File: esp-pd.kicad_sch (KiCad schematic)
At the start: 84 parts, among them J1 USB C Power, J2 USB C Data, J3 Power Out, J4 ESP PD Board pins, Q1 IRF7416, Q2 MMBT3904, SW1 Boot, SW2 Reset, SW3 Up, SW4 Down, SW5 VBUS Switch, U1 ESP32-C3, U2 FUSB302MPX, U3 TPD4E05U06DQA, U4 ME6217C33M5G, U5 MP9943GQ-Z, Y1 40 MHz

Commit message: refactored
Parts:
- removed C13, C14, C15: 10 uF, symbol Device:C
- removed C16, C28: 0.1 uF, symbol Device:C
- removed C19: 22 uF, symbol Device:C
- removed C3, C4: C, symbol Device:C
- removed C5: 1 uF, symbol Device:C
- removed R1, R2: 5.1K, symbol Device:R
- removed R17: 4.7K, symbol Device:R
- removed R18: 1K, symbol Device:R
- removed R19: 1k, symbol Device:R
- removed R20: 10k, symbol Device:R
- removed R7, R8: 10K, symbol Device:R
- added C13, C14, C15: 10 uF, symbol Device:C_Small
- added C16, C4: 0.1 uF, symbol Device:C_Small
- added C3: ~, symbol Device:C_Small
- added C33: 22 uF, symbol Device:C_Small
- added C5: 1 uF, symbol Device:C_Small
- added R1, R8: 5.1k, symbol Device:R_Small
- added R18, R27: 1k, symbol Device:R_Small
- added R19: 10k, symbol Device:R_Small
- added R20: 4.7k, symbol Device:R_Small
- C31: value 1 uF -> ~; now not fitted
- R26: now not fitted
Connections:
- net +5V: now also C13.2, C33.2; no longer C31.2
- net ADC_VBUS: now also C4.2
- net ESP_EN: now also C5.1
- net GND: now also C31.2, J1.S1 (SHIELD), J2.S1 (SHIELD), C13.1, C14.1, C15.1, C16.1, C3.2, C33.1, C4.1, C5.2, R1.2, R19.1, R8.1; no longer C31.1
- net INT: now also R4.1; no longer R6.1
- net MOS_EN: now also R18.1
- net SDA: now also R6.1; no longer R4.1
- net VBUS: now also C15.2, C16.2, R20.1; no longer R10.1
- net VCC: now also R23.1, C14.2; no longer R23.2
- net at L1.1: now also AE1.1 (FEED), C31.1; no longer U1.1 (LNA_IN)
- net at SW5.1, U2.2 (VBUS): now also R10.1
- net D-: now reaches J2.A7 (D-), J2.B7 (D-)
- net D-: now also R25.2, U3.4 (D2+); no longer R24.1, U3.2 (D1-)
- net at Q2.1 (B): now also R18.2, R19.2
- net D+: now reaches J2.A6 (D+), J2.B6 (D+)
- net D+: now also R24.1, U3.5 (D2-); no longer R25.2, U3.1 (D1+)
- net CC1: now reaches J1.A5 (CC1), U2.10 (CC1), U2.11 (CC1)
- net CC1: now also U3.1 (D1+); no longer U3.4 (D2+)
- net CC2: now reaches J1.B5 (CC2), U2.1 (CC2), U2.14 (CC2)
- net CC2: now also U3.2 (D1-); no longer U3.5 (D2-)
- net ANT: now reaches L1.2
- net ANT: now also U1.1 (LNA_IN), C3.1; no longer AE1.1 (FEED)
- net at D2.1 (A), Q1.4 (G): now also R20.2, R27.1
- net at U5.1 (FB): now also R15.2; no longer R15.1
- net at R26.1, U5.8 (PG): now also R23.2; no longer R23.1
- net at J2.B5 (CC2): now also R8.2
- net VOUT: now reaches J3.2 (_VMOS), Q1.5 (D), Q1.6 (D), Q1.7 (D), Q1.8 (D)
- net at J2.A5 (CC1): now also R1.1
- net at C20.1, R14.1, R16.2: now also R15.1; no longer R15.2
- net at Q2.3 (C): now also R27.2
- net Power Good renamed GPIO0
- net SSD_RST: no longer names the net of C27.1, D4.2 (A), OLED1.14 (~{RES}), R22.2
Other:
- note added: "3.3V LDO"
- note added: "5V Buck Regulator"
- note added: "Antenna"
- note added: "Buttons and LED"
- note added: "Connectors"
- note added: "Display"
- note added: "ESP32-C3"
- note added: "For I2C, FUSB INT and ESP32-C3 strapping pins"
- note added: "Pull-ups"
- note added: "USB Data + TVS"
- note added: "USB Power Delivery"
- note added: "VOUT Mosfet"
- moved on the sheet: AE1, C1, C10, C11, C12, C17, C18, C2, C20, C21, C22, C23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

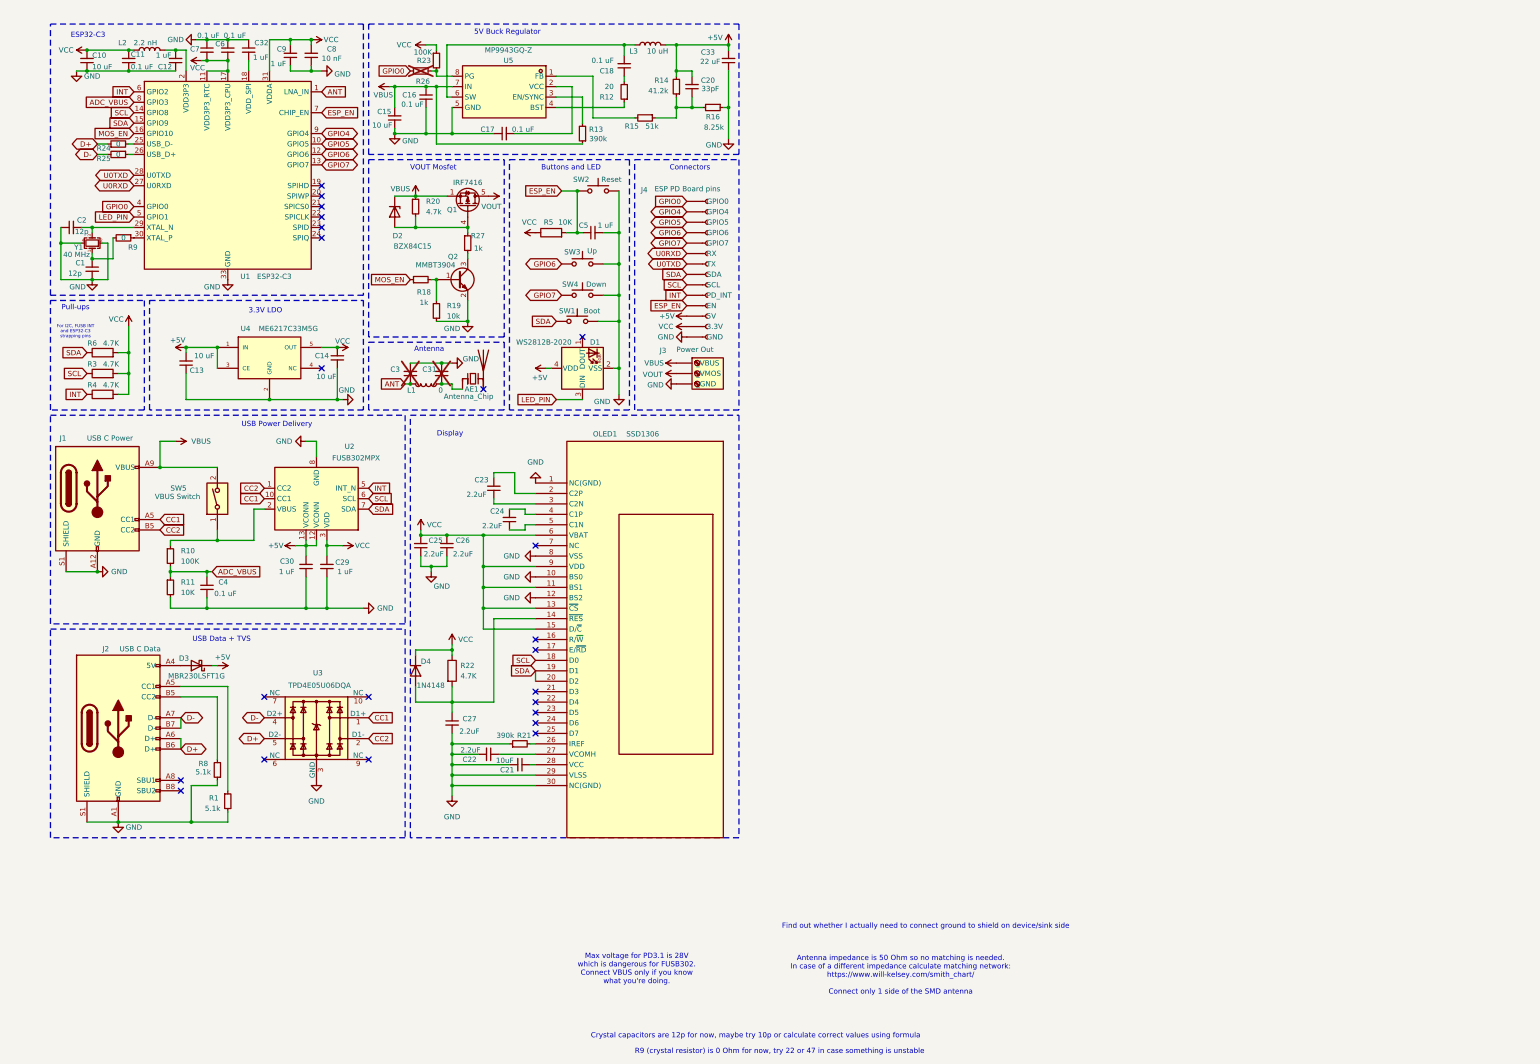
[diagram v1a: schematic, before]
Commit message: A4 format
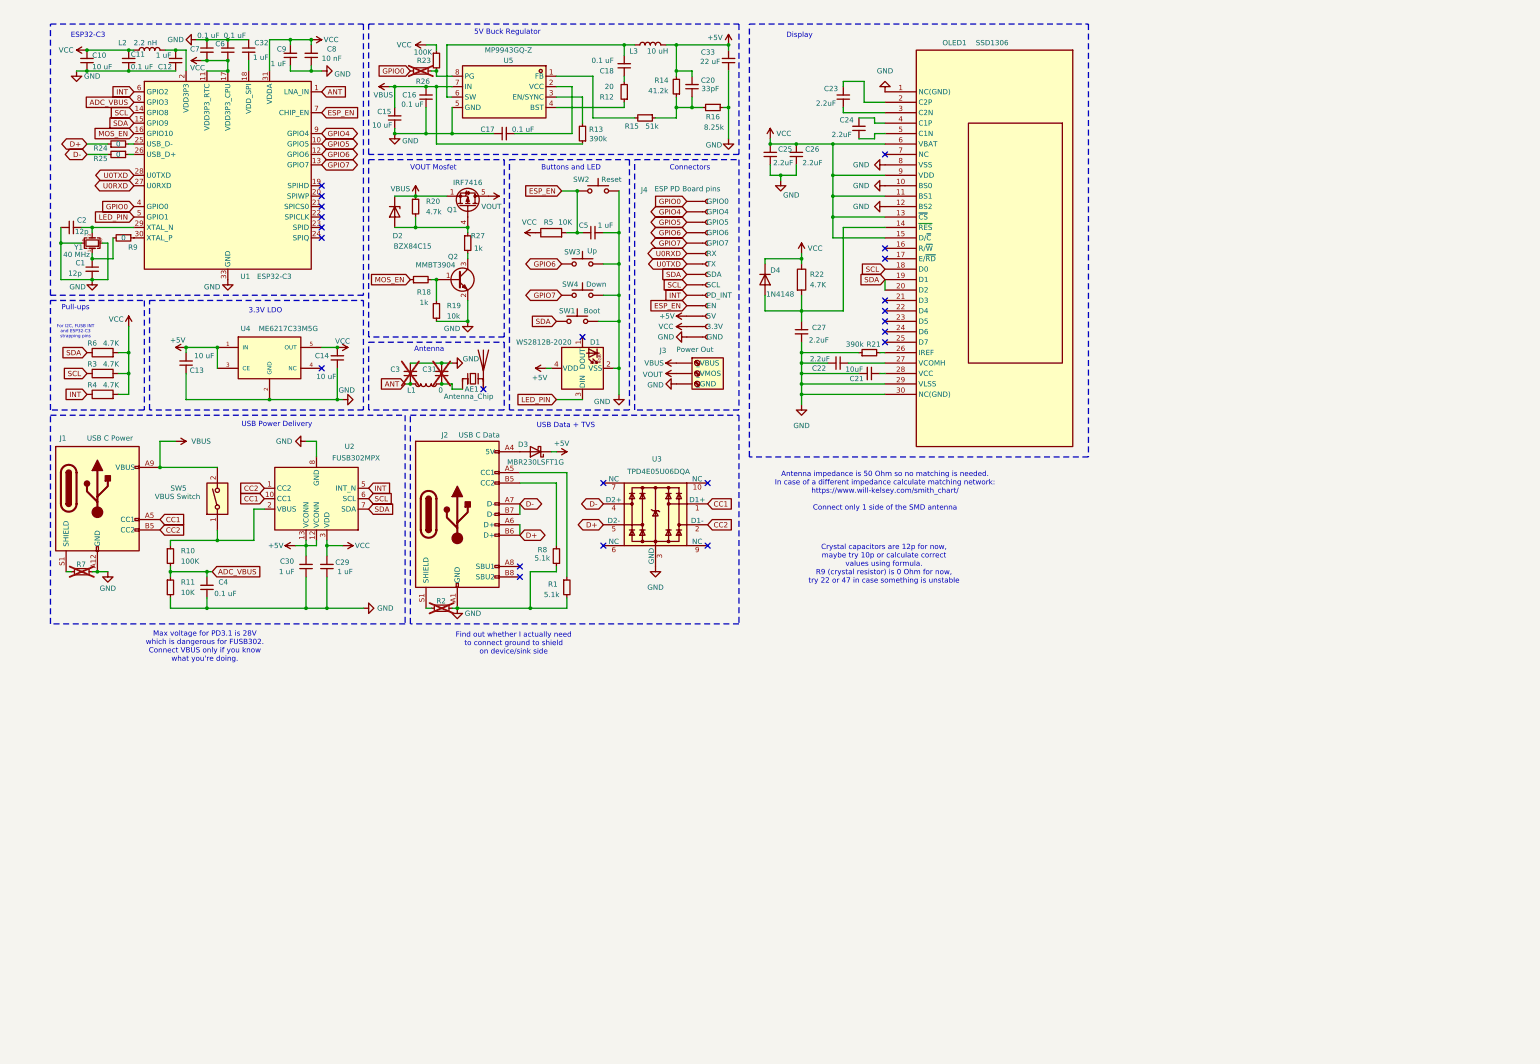
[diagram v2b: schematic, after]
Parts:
- added R2, R7: ~, symbol Device:R_Small
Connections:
- net GND: now also R2.2, R7.2; no longer J1.S1 (SHIELD), J2.S1 (SHIELD)
- new net: J1.S1 (SHIELD), R7.1
- new net: J2.S1 (SHIELD), R2.1
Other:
- note added: "Crystal capacitors are 12p for now, maybe try 10p or calculate correct values using formula. R9 (crystal resistor) is 0 Ohm for now, try 22 or 47 in case something is unstable"
- note removed: "Crystal capacitors are 12p for now, maybe try 10p or calculate correct values using formula"
- note removed: "R9 (crystal resistor) is 0 Ohm for now, try 22 or 47 in case something is unstable"
- moved on the sheet: C21, C22, C23, C24, C25, C26, C27, D3, D4, J2, OLED1, R1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

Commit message: added logos
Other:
- note added: "Notes:"

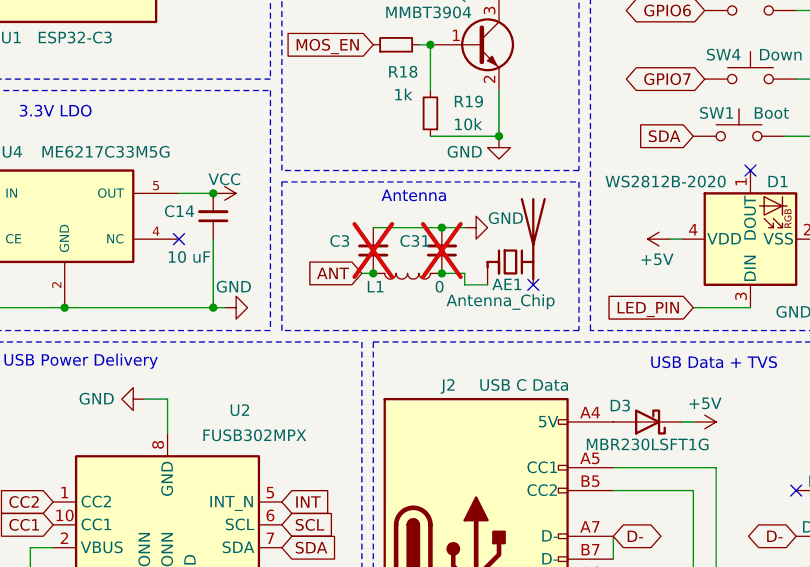
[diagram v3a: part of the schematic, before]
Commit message: footprints partially assigned
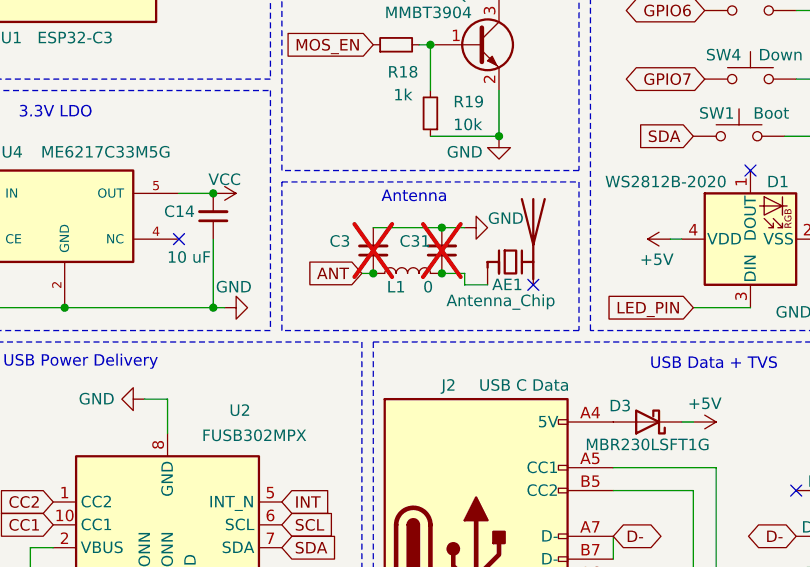
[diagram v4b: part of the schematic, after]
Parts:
- C1, C11, C12, C16, C17, C18, C2, C20, C22, C23, C24, C25, C26, C27, C29, C3, C30, C31, C32, C4, C5, C6, C7, C8, C9: footprint (none) -> Capacitor_SMD:C_0402_1005Metric
- C10, C13, C14, C21, C33: footprint (none) -> Capacitor_SMD:C_0603_1608Metric
- C15: footprint (none) -> Capacitor_SMD:C_1210_3225Metric
- J1: footprint (none) -> Connector_USB:USB_C_Receptacle_GCT_USB4125-xx-x-0190_6P_TopMnt_Horizontal
- J2: footprint (none) -> Connector_USB:USB_C_Receptacle_GCT_USB4105-xx-A_16P_TopMnt_Horizontal
- L1: footprint (none) -> Inductor_SMD:L_0402_1005Metric
- L2: footprint (none) -> Inductor_SMD:L_0603_1608Metric
- L3: footprint (none) -> Inductor_SMD:L_Chilisin_BMRB00060650
- R1, R10, R11, R12, R13, R14, R15, R16, R18, R19, R2, R20, R21, R22, R23, R24, R25, R26, R27, R3, R4, R5, R6, R7, R8, R9: footprint (none) -> Resistor_SMD:R_0402_1005Metric
- SW5: footprint (none) -> Button_Switch_THT:SW_DIP_SPSTx01_Slide_9.78x4.72mm_W7.62mm_P2.54mm
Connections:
- net ANT: now also L1.1; no longer L1.2
- net at AE1.1 (FEED), C31.1: now also L1.2; no longer L1.1
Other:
- moved on the sheet: L1

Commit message: footprints assigned
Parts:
- AE1: footprint (none) -> Inductor_SMD:L_1206_3216Metric
- SW1, SW2, SW3, SW4: footprint (none) -> pb_board:Button SMD 3x4
- Y1: footprint (none) -> Crystal:Crystal_SMD_3225-4Pin_3.2x2.5mm
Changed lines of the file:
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@@
 			)
 		)
-		(property "Footprint" ""
+		(property "Footprint" "pb_board:Button SMD 3x4"
 			(at 153.67 69.85 0)
 			(effects
@@
 			)
 		)
-		(property "Footprint" ""
+		(property "Footprint" "Inductor_SMD:L_1206_3216Metric"
 			(at 124.46 98.425 0)
 			(effects
@@
 			)
 		)
-		(property "Footprint" ""
+		(property "Footprint" "pb_board:Button SMD 3x4"
 			(at 152.4 83.82 0)
 			(effects
@@
 			)
 		)
-		(property "Footprint" ""
+		(property "Footprint" "Crystal:Crystal_SMD_3225-4Pin_3.2x2.5mm"
 			(at 34.29 69.85 0)
 			(effects
@@
 			)
 		)
-		(property "Footprint" ""
+		(property "Footprint" "pb_board:Button SMD 3x4"
 			(at 153.67 77.47 0)
 			(effects
@@
 			)
 		)
-		(property "Footprint" ""
+		(property "Footprint" "pb_board:Button SMD 3x4"
 			(at 157.48 52.07 0)
 			(effects

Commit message: preparing to route PCB x1
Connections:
- net CC1: now also U3.10 (NC)
- net CC2: now also U3.9 (NC)
- net D+: now also U3.6 (NC)
- net D-: now also U3.7 (NC)
- no-connect marks 23 -> 19
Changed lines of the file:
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@@
 	)
 	(no_connect
-		(at 158.75 128.27)
-	)
-	(no_connect
 		(at 90.17 55.88)
 	)
@@
 	)
 	(no_connect
-		(at 158.75 143.51)
-	)
-	(no_connect
-		(at 184.15 143.51)
-	)
-	(no_connect
 		(at 138.43 148.59)
 	)
@@
 	)
 	(no_connect
-		(at 184.15 128.27)
-	)
-	(no_connect
 		(at 90.17 58.42)
 	)
@@
 		)
 	)
+	(global_label "CC1"
+		(shape input)
+		(at 184.15 128.27 0)
+		(fields_autoplaced yes)
+		(effects
+			(font
+				(size 1.27 1.27)
+			)
+			(justify left)
+		)
+		(property "Intersheetrefs" "${INTERSHEET_REFS}"
+			(at 190.8847 128.27 0)
+			(effects
+				(font
+					(size 1.27 1.27)
+				)
+				(justify left)
+				(hide yes)
+			)
+		)
+	)
 	(global_label "GPIO6"
 		(shape bidirectional)
@@
 		)
 	)
+	(global_label "D-"
+		(shape bidirectional)
+		(at 158.75 128.27 180)
+		(fields_autoplaced yes)
+		(effects
+			(font
+				(size 1.27 1.27)
+			)
+			(justify right)
+		)
+		(property "Intersheetrefs" "${INTERSHEET_REFS}"
+			(at 151.8111 128.27 0)
+			(effects
+				(font
+					(size 1.27 1.27)
+				)
+				(justify right)
+				(hide yes)
+			)
+		)
+	)
 	(global_label "ADC_VBUS"
 		(shape input)
@@
 		)
 	)
+	(global_label "CC2"
+		(shape input)
+		(at 184.15 143.51 0)
+		(fields_autoplaced yes)
+		(effects
+			(font
+				(size 1.27 1.27)
+			)
+			(justify left)
+		)
+		(property "Intersheetrefs" "${INTERSHEET_REFS}"
+			(at 190.8847 143.51 0)
+			(effects
+				(font
+					(size 1.27 1.27)
+				)
+				(justify left)
+				(hide yes)
+			)
+		)
+	)
 	(global_label "SCL"
 		(shape input)
@@
 				(hide yes)
 			)
+		)
+	)
+	(global_label "D+"
+		(shape bidirectional)
+		(at 158.75 143.51 180)
+		(fields_autoplaced yes)
+		(effects
+			(font
+				(size 1.27 1.27)
+			)
+			(justify right)
+		)
+		(property "Intersheetrefs" "${INTERSHEET_REFS}"
+			(at 151.8111 143.51 0)
+			(effects
+				(font
+					(size 1.27 1.27)
+				)
+				(justify right)
+				(hide yes)
+			)

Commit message: correct chip antenna footprint
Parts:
- AE1: footprint Inductor_SMD:L_1206_3216Metric -> RF_Antenna:Johanson_2450AT18x100
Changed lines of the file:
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@@
 			)
 		)
-		(property "Footprint" "Inductor_SMD:L_1206_3216Metric"
+		(property "Footprint" "RF_Antenna:Johanson_2450AT18x100"
 			(at 124.46 98.425 0)
 			(effects

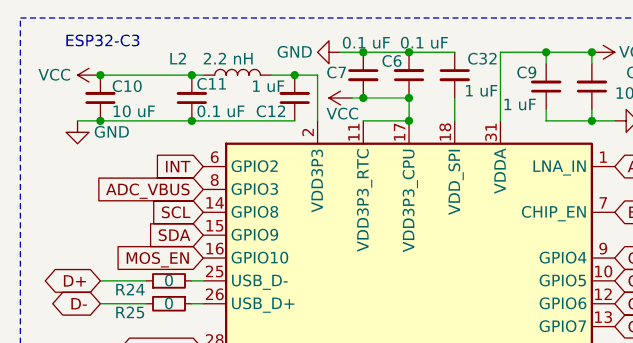
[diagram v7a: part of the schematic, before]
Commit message: edited footprints
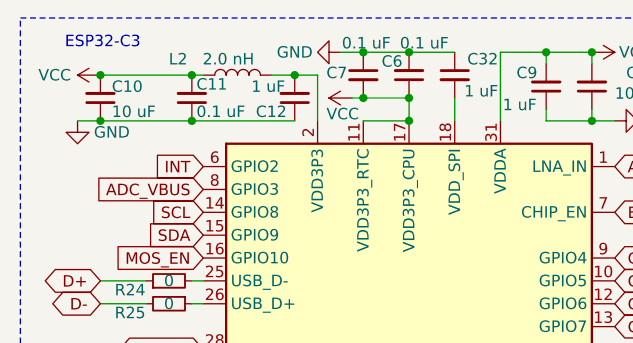
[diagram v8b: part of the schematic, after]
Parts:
- C21: footprint Capacitor_SMD:C_0603_1608Metric -> Capacitor_SMD:C_0402_1005Metric_Pad0.74x0.62mm_HandSolder
- C22, C23, C24, C25, C26, C27: footprint Capacitor_SMD:C_0402_1005Metric -> Capacitor_SMD:C_0402_1005Metric_Pad0.74x0.62mm_HandSolder
- L2: value 2.2 nH -> 2.0 nH; footprint Inductor_SMD:L_0603_1608Metric -> Inductor_SMD:L_0402_1005Metric
- R21, R22: footprint Resistor_SMD:R_0402_1005Metric -> Resistor_SMD:R_0402_1005Metric_Pad0.72x0.64mm_HandSolder
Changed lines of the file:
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@@
 			)
 		)
-		(property "Value" "2.2 nH"
+		(property "Value" "2.0 nH"
 			(at 47.244 21.082 90)
 			(effects
@@
 			)
 		)
-		(property "Footprint" "Inductor_SMD:L_0603_1608Metric"
+		(property "Footprint" "Inductor_SMD:L_0402_1005Metric"
 			(at 48.26 22.86 0)
 			(effects
@@
 			)
 		)
-		(property "Footprint" "Capacitor_SMD:C_0402_1005Metric"
+		(property "Footprint" "Capacitor_SMD:C_0402_1005Metric_Pad0.74x0.62mm_HandSolder"
 			(at 205.74 48.26 0)
 			(effects
@@
 			)
 		)
-		(property "Footprint" "Capacitor_SMD:C_0402_1005Metric"
+		(property "Footprint" "Capacitor_SMD:C_0402_1005Metric_Pad0.74x0.62mm_HandSolder"
 			(at 207.01 91.44 0)
 			(effects
@@
 			)
 		)
-		(property "Footprint" "Capacitor_SMD:C_0402_1005Metric"
+		(property "Footprint" "Capacitor_SMD:C_0402_1005Metric_Pad0.74x0.62mm_HandSolder"
 			(at 217.17 34.29 0)
 			(effects
@@
 			)
 		)
-		(property "Footprint" "Capacitor_SMD:C_0402_1005Metric"
+		(property "Footprint" "Capacitor_SMD:C_0402_1005Metric_Pad0.74x0.62mm_HandSolder"
 			(at 215.9 99.06 0)
 			(effects
@@
 			)
 		)
-		(property "Footprint" "Resistor_SMD:R_0402_1005Metric"
+		(property "Footprint" "Resistor_SMD:R_0402_1005Metric_Pad0.72x0.64mm_HandSolder"
 			(at 205.232 78.74 90)
 			(effects
@@
 			)
 		)
-		(property "Footprint" "Capacitor_SMD:C_0402_1005Metric"
+		(property "Footprint" "Capacitor_SMD:C_0402_1005Metric_Pad0.74x0.62mm_HandSolder"
 			(at 199.39 48.26 0)
 			(effects
@@
 			)
 		)
-		(property "Footprint" "Capacitor_SMD:C_0402_1005Metric"
+		(property "Footprint" "Capacitor_SMD:C_0402_1005Metric_Pad0.74x0.62mm_HandSolder"
 			(at 220.98 41.91 0)
 			(effects
@@
 			)
 		)
-		(property "Footprint" "Capacitor_SMD:C_0603_1608Metric"
+		(property "Footprint" "Capacitor_SMD:C_0402_1005Metric_Pad0.74x0.62mm_HandSolder"
 			(at 223.52 101.6 0)
 			(effects
@@
 			)
 		)
-		(property "Footprint" "Resistor_SMD:R_0402_1005Metric"
+		(property "Footprint" "Resistor_SMD:R_0402_1005Metric_Pad0.72x0.64mm_HandSolder"
 			(at 223.52 96.52 0)
 			(effects
